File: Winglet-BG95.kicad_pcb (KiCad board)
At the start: 4 copper layers, 30 x 47.6 mm, 39 parts, among them J1 A-1JB, J2 A-1JB, J3 1042240820, M1 Mount_M2.5, M2 Mount_M2.5, Q1 DMG1012UW-7, Q2 DMG1013UW-7, Q3 DMG1012UW-7, U1 BG95MxLA, U2 MFF2-SIM, U3 24AA01T-I/OT, U4 FXLA108BQX

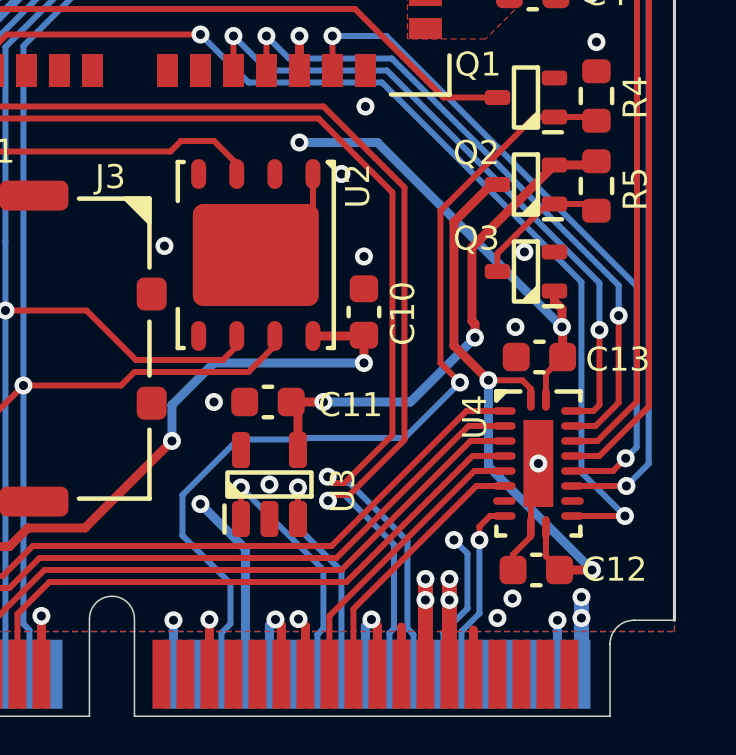
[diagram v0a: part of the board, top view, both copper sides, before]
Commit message: Add TP for VDDA
Change board color to blue
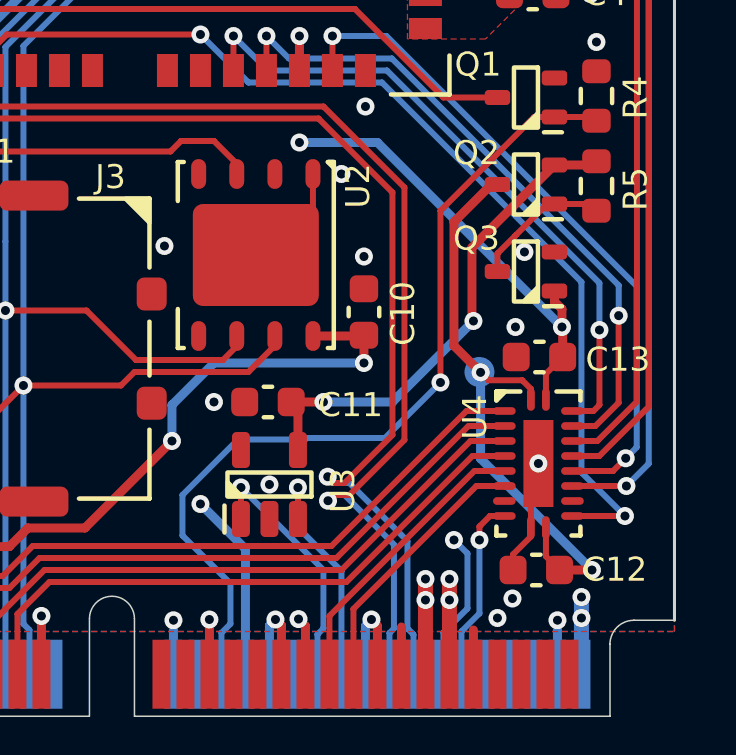
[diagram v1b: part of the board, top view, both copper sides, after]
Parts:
- added TP2: ~, N_NonPart:TestPoint_1mm, B.Cu at (73.5, 89.3)
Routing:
- net /Connector/RESET: track 30.1 -> 29.2 mm

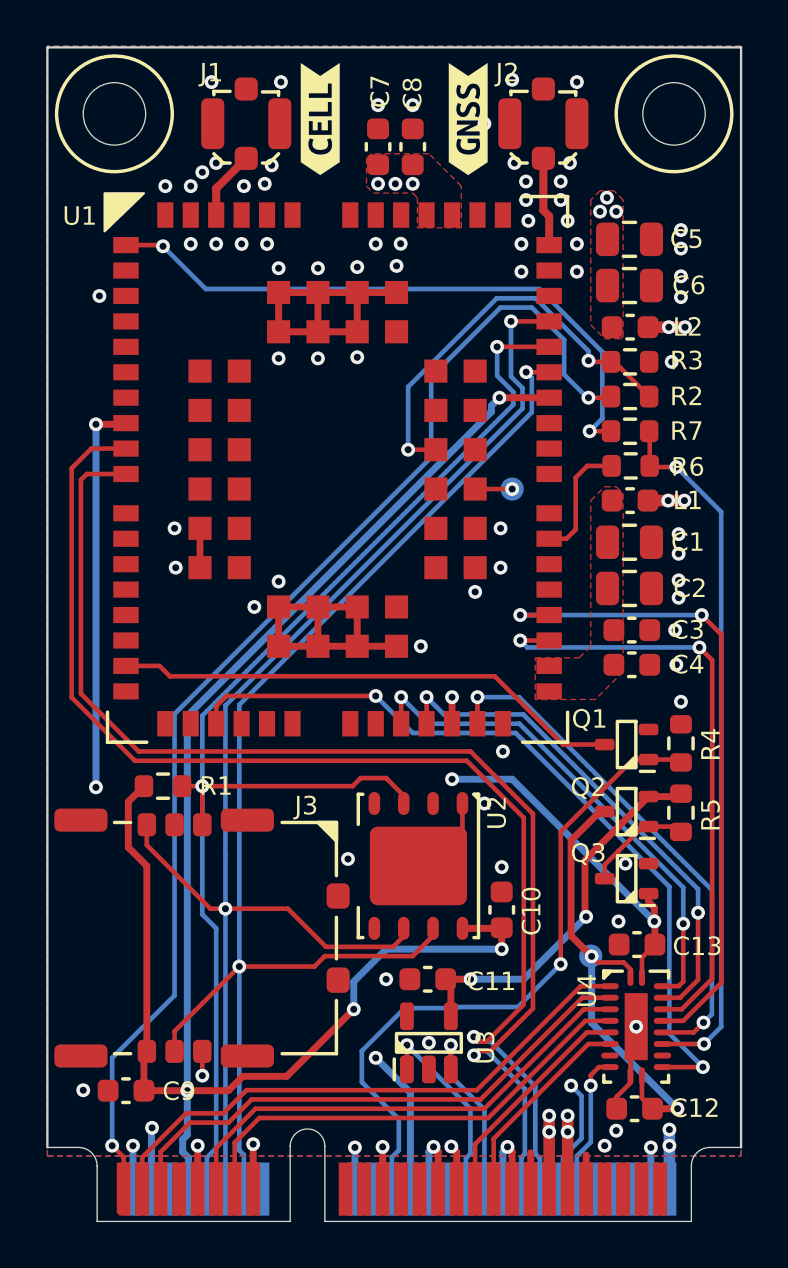
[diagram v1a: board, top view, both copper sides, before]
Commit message: Remove PON_TRIG key, add PWRKEY control.
Remove USIM options on PCIE interface.
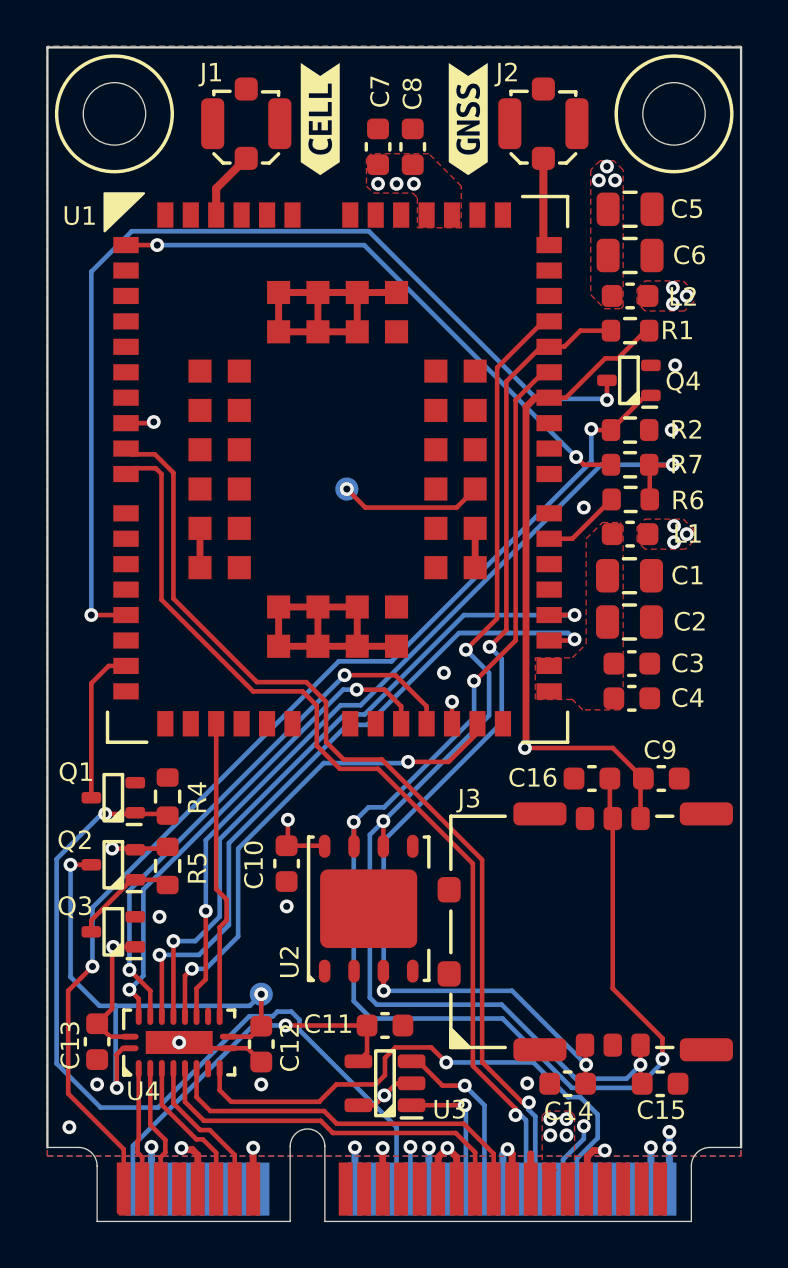
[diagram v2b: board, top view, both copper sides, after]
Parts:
- removed R3: 10K, R_Resistor:R_0603
- added C14: 100n, C_Capacitor:C_0603, F.Cu at (72.5, 94.8)
- added C15: 100n, C_Capacitor:C_0603, F.Cu at (76.5, 94.8)
- added C16: 100n, C_Capacitor:C_0603, F.Cu at (73.5, 81.6)
- added Q4: DMG1012UW-7, U_IC:SC70-3, F.Cu at (75.2, 64.4)
- C4, C8: value 100p -> 100n
- R2: value 10K -> 100K
- moved R1 28.2 mm to (75.2, 62.2), turned to 180 degrees
- moved C9 26.8 mm to (76.5, 81.6), turned to 0 degrees
- moved C13 23.7 mm to (52.1, 93.0), turned to -90 degrees
- moved R4 22.3 mm to (55.2, 82.4)
- moved R5 22.3 mm to (55.2, 85.4)
- moved Q1 22.3 mm to (52.9, 82.5)
- moved Q2 22.3 mm to (52.9, 85.3)
- moved Q3 22.3 mm to (52.9, 88.2)
- moved U4 19.8 mm to (55.7, 93.0), turned to 90 degrees
- moved J3 16.6 mm to (73.2, 88.2), turned to 90 degrees
- moved C12 16.4 mm to (59.2, 93.1), turned to -90 degrees
- moved TP2 14.3 mm to (59.2, 91.0), turned to 90 degrees
- moved C10 9.52 mm to (60.3, 85.3), turned to -90 degrees
- moved TP1 7.15 mm to (63.0, 69.1)
- moved U2 2.84 mm to (63.9, 87.2), turned to 90 degrees
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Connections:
- C10 pad 1: /USIM_VDD -> /Memory/USIM_VDD
- C9 pad 1: /USIM_VDD -> /Memory/USIM_VDD
- J3 pad C1: /USIM_VDD -> /Memory/USIM_VDD
- J3 pad C2: /USIM_RST -> /Memory/USIM_RST
- J3 pad C3: /USIM_CLK -> /Memory/USIM_CLK
- J3 pad C7: /USIM_DATA -> /Memory/USIM_DATA
- N1 pad 10: /USIM_DATA -> unconnected-(N1-Pad10)
- N1 pad 12: /USIM_CLK -> unconnected-(N1-Pad12)
- N1 pad 14: /USIM_RST -> unconnected-(N1-Pad14)
- N1 pad 8: /USIM_VDD -> unconnected-(N1-Pad8)
- R1 pad 1: /USIM_VDD -> /Memory/USIM_VDD
- R1 pad 2: /USIM_DATA -> /Memory/USIM_DATA
- R2 pad 2: /Modem/MODEM_PON -> GND
- U1 pad 15: unconnected-(U1A-PWRKEY-Pad15) -> /Modem/MODEM_PWRKEY
- U1 pad 43: /USIM_VDD -> /Memory/USIM_VDD
- U1 pad 44: /USIM_RST -> /Memory/USIM_RST
- U1 pad 45: /USIM_DATA -> /Memory/USIM_DATA
- U1 pad 46: /USIM_CLK -> /Memory/USIM_CLK
- U1 pad 96: /Modem/MODEM_PON -> unconnected-(U1A-PON_TRIG-Pad96)
- U2 pad 3: /USIM_DATA -> /Memory/USIM_DATA
- U2 pad 6: /USIM_CLK -> /Memory/USIM_CLK
- U2 pad 7: /USIM_RST -> /Memory/USIM_RST
- U2 pad 8: /USIM_VDD -> /Memory/USIM_VDD
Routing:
- net /USIM_VDD: track 77.3 -> 0.00 mm, vias 4 -> 0
- net /Memory/USIM_RST: track 0.00 -> 60.9 mm, vias 0 -> 3
- net /USIM_CLK: track 59.0 -> 0.00 mm, vias 2 -> 0
- net /USIM_DATA: track 57.3 -> 0.00 mm, vias 2 -> 0
- net /USIM_RST: track 56.0 -> 0.00 mm, vias 2 -> 0
- net /Memory/USIM_CLK: track 0.00 -> 49.7 mm, vias 0 -> 3
- net /Memory/USIM_DATA: track 0.00 -> 46.9 mm, vias 0 -> 3
- net /Memory/USIM_VDD: track 0.00 -> 43.4 mm, vias 0 -> 2
- net /Modem/MODEM_PWRKEY: track 0.00 -> 43.2 mm, vias 0 -> 2
- net /Modem/MODEM_NETLIGHT: track 34.1 -> 13.0 mm, vias 2 -> 0
- net /Connector/GNSS_RX: track 24.7 -> 5.31 mm
- net /Connector/GNSS_TX: track 23.8 -> 5.56 mm
- net /Modem/MODEM_PON: track 17.9 -> 0.00 mm, vias 2 -> 0
- net /Connector/NETLIGHT: track 6.15 -> 23.7 mm
- net /Modem/MODEM_RESET: track 22.1 -> 6.76 mm
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- added copper zone on F.Cu, net +BATT

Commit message: Lay out PCB
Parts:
- moved Q4 31.5 mm to (52.2, 86.0)
- moved R2 28.4 mm to (54.5, 86.0), turned to 90 degrees
- moved ~ 15.5 mm to (64.3, 61.6), turned to 180 degrees
- moved Q2 3.61 mm to (52.2, 88.9)
- moved R5 3.61 mm to (54.5, 89.0)
- moved Q3 3.61 mm to (52.2, 91.8)
- moved TP1 2.53 mm to (65.3, 69.9)
- moved C13 1.79 mm to (52.7, 94.7)
- moved C5 1.55 mm to (75.2, 58.5)
- moved C6 1.55 mm to (75.2, 60.5)
- moved L2 1.55 mm to (75.2, 62.3)
- moved R1 1.55 mm to (75.2, 63.8)
- moved C12 1.18 mm to (60.2, 93.8)
- moved TP2 1.18 mm to (60.2, 91.7)
- moved U4 1.18 mm to (56.6, 93.7)
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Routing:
- net /Connector/WAKE: track 47.7 -> 17.0 mm, vias 2 -> 0
- net /Modem/MODEM_PWRKEY: track 43.2 -> 13.5 mm, vias 2 -> 0
- net /Memory/USIM_RST: track 60.9 -> 37.4 mm
- net /Connector/RESET: track 36.8 -> 24.8 mm
- net /Translation/VCCA: track 23.4 -> 18.3 mm
- net /Memory/USIM_CLK: track 49.7 -> 45.1 mm
- net /Modem/MODEM_DTR: track 21.4 -> 26.0 mm
- net /Memory/USIM_VDD: track 43.4 -> 47.5 mm
- net /Connector/USB_VBUS: track 45.2 -> 41.1 mm, vias 2 -> 1
- net /Memory/USIM_DATA: track 46.9 -> 50.6 mm
- net +VDDIO: track 30.4 -> 33.4 mm
- net Net-(U1A-USB_BOOT): track 6.21 -> 3.48 mm
- net /Connector/NETLIGHT: track 23.7 -> 21.1 mm
- net +1V8: track 29.8 -> 32.4 mm
- net /Connector/TX: track 6.55 -> 5.21 mm
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
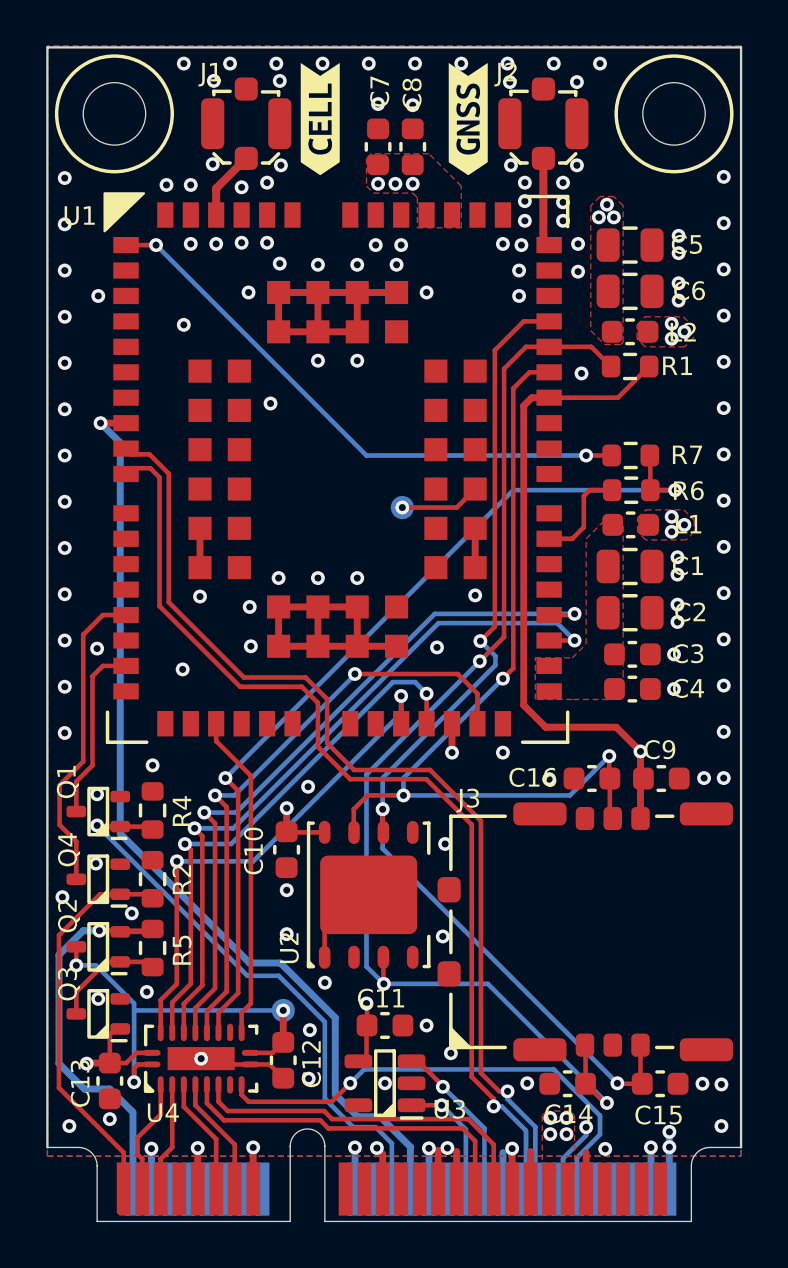
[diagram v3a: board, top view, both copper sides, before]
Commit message: Added tooling holes
Updated the readme
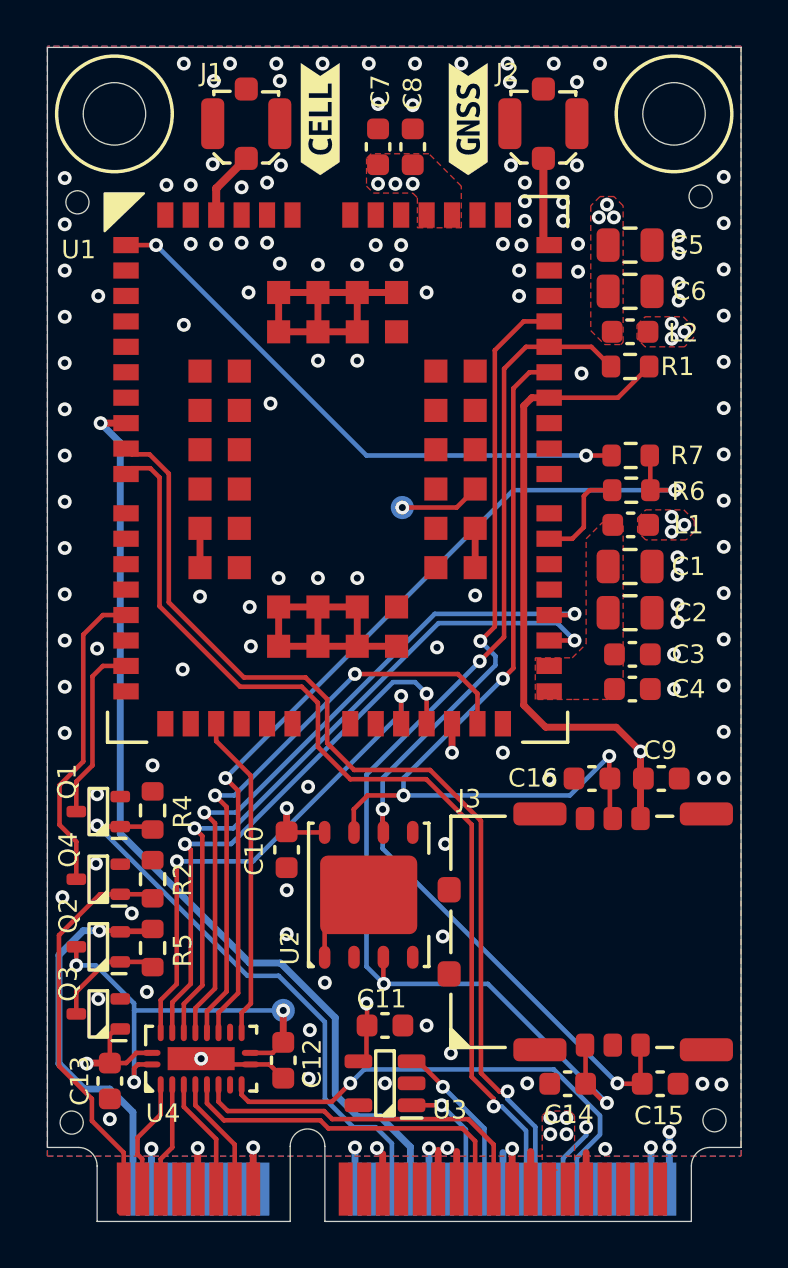
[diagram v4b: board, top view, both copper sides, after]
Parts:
- added N2: ToolingHole, N_NonPart:ToolingHole_1mm, F.Cu at (78.2, 56.5)
- added N3: ToolingHole, N_NonPart:ToolingHole_1mm, F.Cu at (51.0, 96.5)
- added N4: ToolingHole, N_NonPart:ToolingHole_1mm, F.Cu at (51.3, 56.7)
- added N5: ToolingHole, N_NonPart:ToolingHole_1mm, F.Cu at (78.8, 96.4)
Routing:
- net GND: vias 140 -> 138

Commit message: Implement fixes
Closes #2
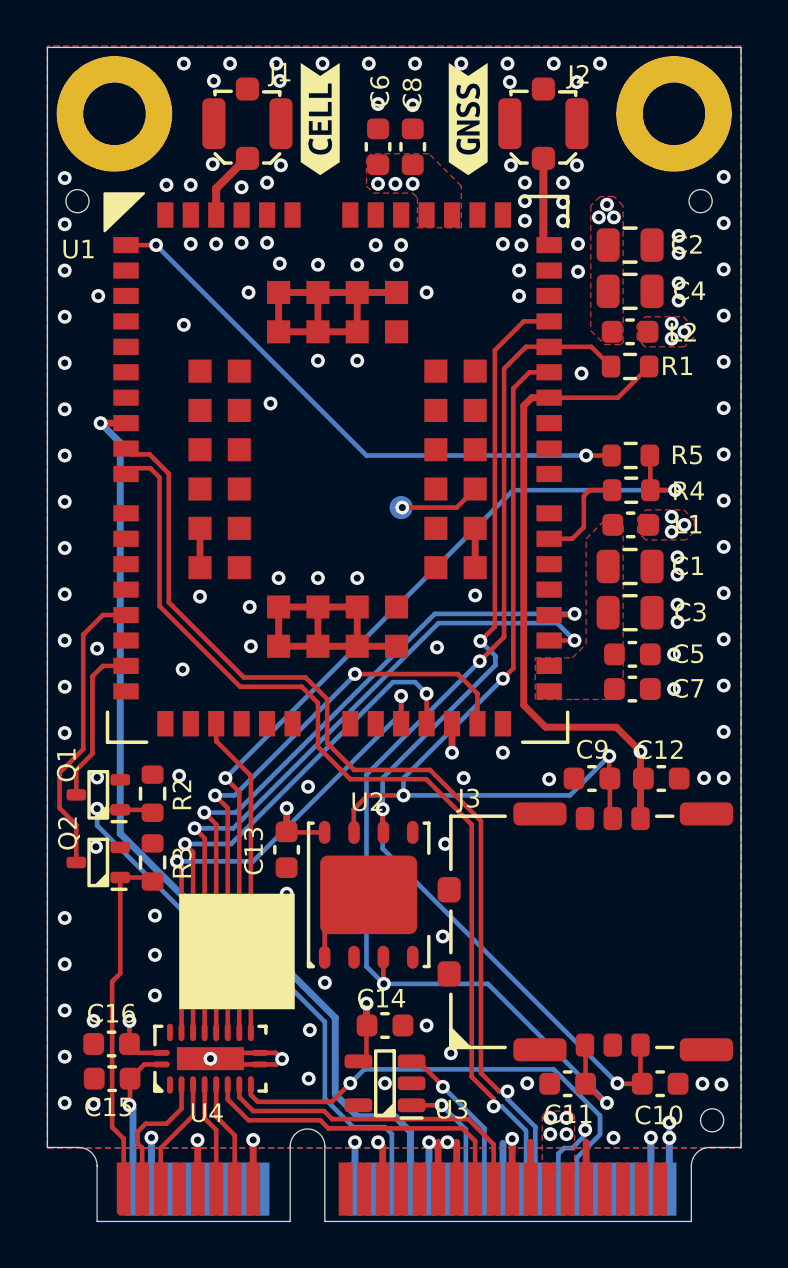
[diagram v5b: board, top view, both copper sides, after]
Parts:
- removed the N5 at (78.8, 96.4)
- removed the Q2 at (52.2, 88.9)
- removed Q3: DMG1012UW-7, U_IC:SC70-3
- removed the R5 at (54.5, 89.0)
- removed TP2: ~, N_NonPart:TestPoint_1mm
- added N1: QR 5mm, N_NonPart:QR_5mm_JLC, F.Cu at (58.2, 89.1)
- C10: renamed from C15; value 100n -> 33p
- C11: renamed from C14; value 100n -> 33p
- C7: renamed from C4; value 100n -> 33p
- C8: value 100n -> 33p
- C9: renamed from C16; value 100n -> 33p
- J1, J2: value A-1JB -> 2337019-1
- M1, M2: value Mount_M2.5 -> PTH_M2.5; footprint M_Mechanical:Mount_M2.5 -> M_Mechanical:PTH_M2.5
- TP1: footprint N_NonPart:TestPoint_1mm -> TP_TestPoint:TestPoint_1mm
- moved N3 27.7 mm to (78.8, 96.4)
- moved C15 7.44 mm to (52.8, 94.6), turned to 180 degrees
- moved C16 1.60 mm to (52.8, 93.1), turned to 180 degrees
- moved Q1 0.72 mm to (52.2, 82.3)
- moved Q2 0.72 mm to (52.2, 85.2)
- moved R2 0.72 mm to (54.5, 82.3)
- moved R3 0.72 mm to (54.5, 85.2)
- moved U4 0.40 mm to (57.0, 93.7)
- moved N2 0.20 mm to (78.2, 56.6)
- moved N4 0.05 mm to (51.3, 56.6)
- turned TP1 to 180 degrees
- renumbered C9 to C12, C10 to C13, C11 to C14, C12 to C15, C13 to C16, C5 to C2, C2 to C3, C6 to C4, C3 to C5, C7 to C6, N1 to N5, Q4 to Q2, R4 to R2, R2 to R3, R6 to R4, R7 to R5
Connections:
- C15 pad 1: /Translation/VCCA -> +VDDIO
- R4 pad 2: Net-(U4-B5) -> Net-(U4-B6)
- R5 pad 2: Net-(U4-B5) -> Net-(U4-B6)
- U4 pad 1: /Translation/VCCA -> +VDDIO
- U4 pad 11: /Translation/VCCA -> GND
- U4 pad 13: unconnected-(U4-B6-Pad13) -> Net-(U4-B6)
- U4 pad 14: Net-(U4-B5) -> /Modem/MODEM_DTR
- U4 pad 15: /Modem/MODEM_DTR -> /Modem/MODEM_TX
- U4 pad 16: /Modem/MODEM_TX -> /Modem/MODEM_RX
- U4 pad 17: /Modem/MODEM_RX -> /Modem/MODEM_GNSS_TX
- U4 pad 18: /Modem/MODEM_GNSS_TX -> /Modem/MODEM_GNSS_RX
- U4 pad 19: /Modem/MODEM_GNSS_RX -> unconnected-(U4-B0-Pad19)
- U4 pad 2: /Connector/GNSS_RX -> unconnected-(U4-A0-Pad2)
- U4 pad 3: /Connector/GNSS_TX -> /Connector/GNSS_RX
- U4 pad 4: /Connector/RX -> /Connector/GNSS_TX
- U4 pad 5: /Connector/TX -> /Connector/RX
- U4 pad 6: /Connector/DTR -> /Connector/TX
- U4 pad 7: /Connector/DCD -> /Connector/DTR
- U4 pad 8: unconnected-(U4-A6-Pad8) -> /Connector/DCD
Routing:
- net Net-(U4-B5): track 38.8 -> 0.00 mm, vias 2 -> 0
- net Net-(U4-B6): track 0.00 -> 38.4 mm, vias 0 -> 2
- net /Translation/VCCA: track 18.3 -> 0.00 mm, vias 3 -> 0
- net +VDDIO: track 33.4 -> 22.0 mm
- net GND: track 64.0 -> 71.1 mm, vias 138 -> 145
- net +1V8: track 32.4 -> 26.9 mm
- net Net-(Q2-G): track 4.88 -> 0.00 mm
- net /Connector/WAKE: track 17.0 -> 15.3 mm
- net /Connector/DCD: track 15.3 -> 14.3 mm
- net /Connector/DTR: track 15.1 -> 14.2 mm
- net /Connector/RESET: track 24.8 -> 25.8 mm
- net /Connector/GNSS_RX: track 5.00 -> 5.90 mm
- net /Modem/MODEM_PWRKEY: track 13.5 -> 12.8 mm
- net /Modem/MODEM_RESET: track 7.78 -> 7.05 mm
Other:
- board text added: "Winglet-BG95 v1.1 Jun 25"
- board text removed: "Winglet-BG95 v1.0 Aug 24"
